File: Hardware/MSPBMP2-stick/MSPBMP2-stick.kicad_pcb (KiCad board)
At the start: 2 copper layers, 51.5 x 20 mm, 54 parts, among them J1 48037-0001, J2 JTAG, J3 SWD, U1 STM32L432KBU6, U2 LD1117AG-33-AB3-A-R, U3 AD8531ARTZ, U4 TXS0108EPWR, Y1 32768

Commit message: Schema update of PCB-Stick
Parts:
- removed the C2 at (85.0, 61.8)
- removed the R11 at (104.6, 68.8)
- removed the R7 at (85.0, 60.8)
- added C6: 220nF, Capacitor_SMD:C_0402_1005Metric_Pad0.74x0.62mm_HandSolder, F.Cu at (85.0, 62.8)
- added R4: 100, Resistor_SMD:R_0402_1005Metric_Pad0.72x0.64mm_HandSolder, F.Cu at (85.0, 61.8)
- C1: value 220nF -> 100nF
- C12: renamed from C10; value 1.2pF -> 4.7pF
- C13: renamed from C11; value 1.2pF -> 4.7pF
- RN1, RN2: footprint Resistor_SMD:R_Array_Convex_4x0402 -> LocalLib:R_Array_Convex_4x0402_hand_soldered
- U1: renamed from U2; value LD1117AG-33-AB3-A-R -> AMS1117-3.3
- U3: footprint Package_TO_SOT_SMD:TSOT-23-5_HandSoldering -> Package_TO_SOT_SMD:SOT-23-5_HandSoldering
- Y1: value 32768 -> 32768 7pF
- moved C16 4.27 mm to (96.2, 66.3), turned to 0 degrees
- moved C15 4.16 mm to (96.8, 67.5), turned to 0 degrees
- moved C19 1.54 mm to (96.1, 56.8)
- moved C17 1.23 mm to (95.5, 55.5)
- moved NT1 1.07 mm to (87.1, 62.8)
- moved F1 0.60 mm to (103.0, 56.5)
- moved C23 0.29 mm to (77.9, 54.1)
- moved U4 0.06 mm to (102.4, 64.7), turned to 180 degrees
- renumbered C13 to C10, C8 to C11, C3 to C2, C4 to C3, C6 to C4, C9 to C5, C12 to C7, C5 to C8, C7 to C9, R2 to R1, R10 to R11, R3 to R2, R1 to R3, R4 to R5, R5 to R7, R9 to R8, R8 to R9, U1 to U2
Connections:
- C15 pad 1: +3V3 -> GND
- C15 pad 2: GND -> +3V3
- C16 pad 1: +3V3 -> GND
- C16 pad 2: GND -> +3V3
- RN1 pad 1: Net-(RN1-Pad1) -> /LTDO
- RN1 pad 2: Net-(RN1-Pad2) -> /LTDI
- RN1 pad 3: Net-(RN1-Pad3) -> /LTMS
- RN1 pad 4: Net-(RN1-Pad4) -> /LTCK
- RN2 pad 1: Net-(RN2-Pad1) -> /LTEST
- RN2 pad 2: Net-(RN2-Pad2) -> /LRST
- RN2 pad 3: Net-(RN2-Pad3) -> /LTXD
- RN2 pad 4: Net-(RN2-Pad4) -> /LRXD
- U2 pad 15: /JENA -> Net-(U2-Pad15)
- U4 pad 1: /JTDO -> /LRXD
- U4 pad 10: /JENA -> /VCC_TOOL
- U4 pad 12: Net-(RN2-Pad4) -> /JTDO
- U4 pad 13: Net-(RN2-Pad3) -> /JTDI
- U4 pad 14: Net-(RN2-Pad2) -> /JTMS
- U4 pad 15: Net-(RN2-Pad1) -> /JTCK
- U4 pad 16: Net-(RN1-Pad4) -> /JTEST
- U4 pad 17: Net-(RN1-Pad3) -> /JRST
- U4 pad 18: Net-(RN1-Pad2) -> /JTXD
- U4 pad 19: /VCC_TOOL -> +3V3
- U4 pad 2: +3V3 -> /VCC_TOOL
- U4 pad 20: Net-(RN1-Pad1) -> /JRXD
- U4 pad 3: /JTDI -> /LTXD
- U4 pad 4: /JTMS -> /LRST
- U4 pad 5: /JTCK -> /LTEST
- U4 pad 6: /JTEST -> /LTCK
- U4 pad 7: /JRST -> /LTMS
- U4 pad 8: /JRXD -> /LTDI
- U4 pad 9: /JTXD -> /LTDO
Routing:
- net /JENA: track 33.3 -> 0.00 mm, vias 2 -> 0
- net GND: track 44.0 -> 37.3 mm, vias 16 -> 15
- net Net-(RN1-Pad2): track 4.36 -> 0.00 mm
- net Net-(RN1-Pad3): track 4.30 -> 0.00 mm
- net /VCC_TOOL: track 20.4 -> 24.6 mm
- net Net-(RN1-Pad4): track 4.17 -> 0.00 mm
- net /LTMS: track 0.00 -> 4.17 mm
- net /LTCK: track 0.00 -> 4.11 mm
- net /LTDI: track 0.00 -> 4.10 mm
- net /LTDO: track 0.00 -> 3.90 mm
- net +3V3: track 111.0 -> 114.3 mm
- net Net-(RN1-Pad1): track 3.20 -> 0.00 mm
- net /LRXD: track 0.00 -> 2.71 mm
- net Net-(RN2-Pad4): track 2.49 -> 0.00 mm
- net Net-(RN2-Pad1): track 2.47 -> 0.00 mm
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
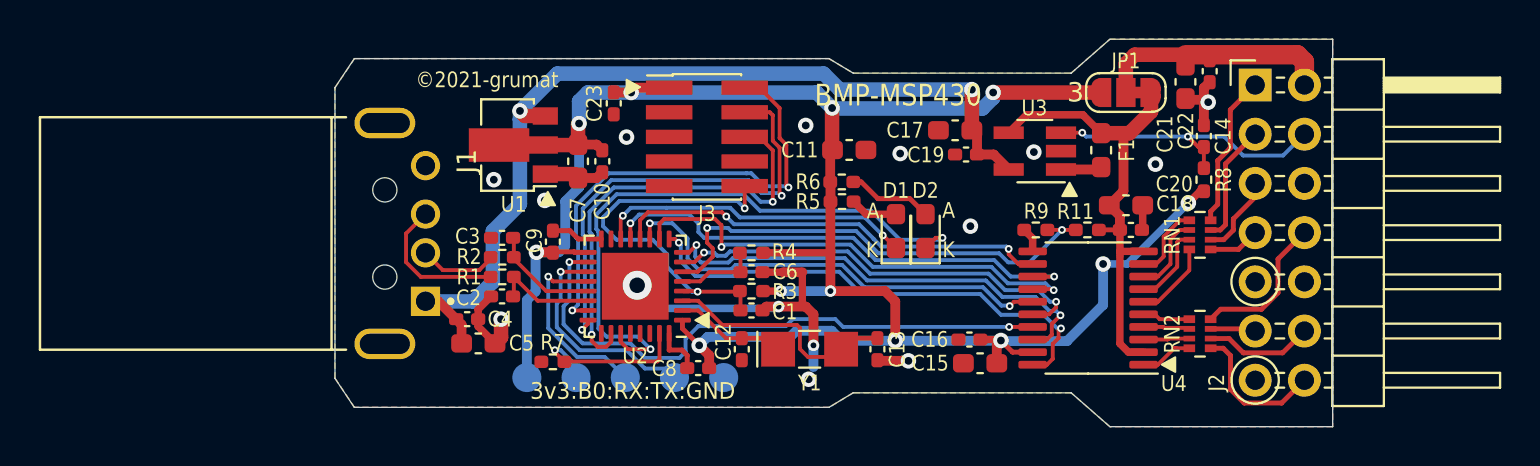
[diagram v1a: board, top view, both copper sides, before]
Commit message: Hardware V2 improvements (component values and sizes, layout and review of V-Target circuitry).
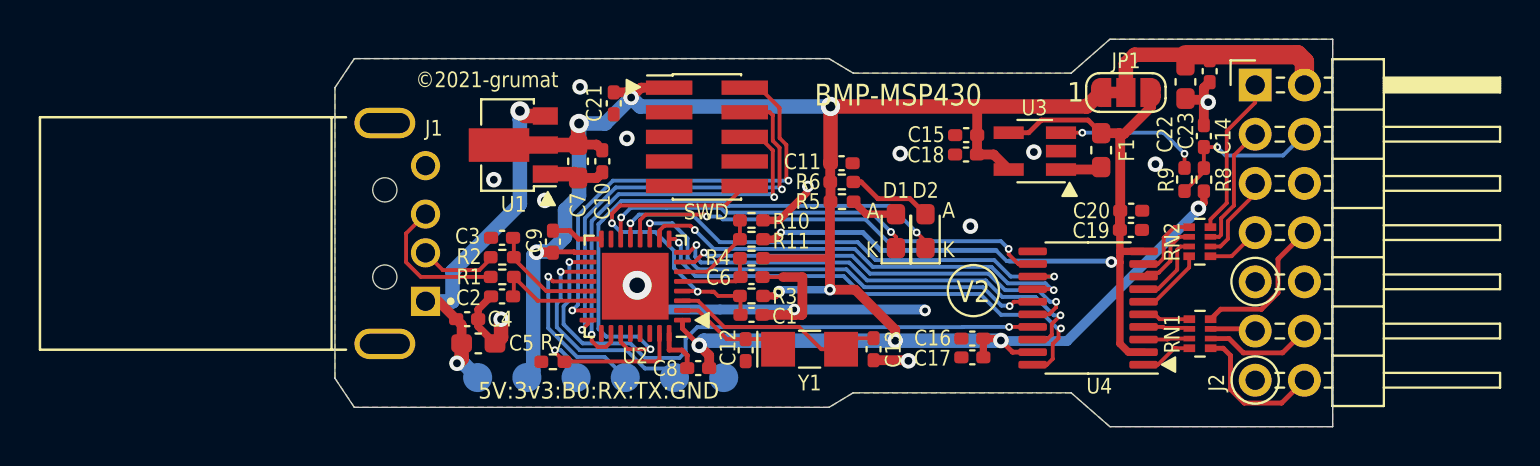
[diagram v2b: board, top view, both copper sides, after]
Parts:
- added R9: 4k7, Resistor_SMD:R_0402_1005Metric_Pad0.72x0.64mm_HandSolder, F.Cu at (107.3, 58.0)
- added TP1: 5V, TestPoint:TestPoint_Pad_D1.5mm, B.Cu at (70.9, 68.3)
- C11, C20: value 22uF -> 10uF; footprint Capacitor_SMD:C_0603_1608Metric_Pad1.08x0.95mm_HandSolder -> Capacitor_SMD:C_0402_1005Metric_Pad0.74x0.62mm_HandSolder
- C15: renamed from C17; value 22uF -> 10uF; footprint Capacitor_SMD:C_0603_1608Metric_Pad1.08x0.95mm_HandSolder -> Capacitor_SMD:C_0402_1005Metric_Pad0.74x0.62mm_HandSolder
- C16: renamed from C15; value 22uF -> 10uF; footprint Capacitor_SMD:C_0603_1608Metric_Pad1.08x0.95mm_HandSolder -> Capacitor_SMD:C_0402_1005Metric_Pad0.74x0.62mm_HandSolder
- moved R11 17.3 mm to (85.0, 61.1)
- moved R10 14.7 mm to (85.0, 60.1), turned to 0 degrees
- moved C16 1.34 mm to (96.4, 66.2)
- moved C17 0.93 mm to (96.4, 67.2)
- moved C11 0.79 mm to (89.7, 57.2)
- moved C15 0.62 mm to (96.1, 55.8)
- moved C20 0.39 mm to (104.6, 59.6)
- moved RN2 0.35 mm to (108.1, 61.2)
- moved R4 0.27 mm to (85.0, 62.1)
- moved C6 0.25 mm to (85.0, 63.1)
- moved NT1 0.25 mm to (87.1, 63.1)
- moved R3 0.25 mm to (85.0, 64.0)
- moved C1 0.23 mm to (85.0, 65.0)
- moved C12 0.21 mm to (84.7, 66.8)
- moved C13 0.20 mm to (91.3, 66.8)
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- renumbered C16 to C17, C19 to C18, C18 to C19, C23 to C21, C21 to C22, C22 to C23, R9 to R10, RN2 to RN1, RN1 to RN2, TP1 to TP2, TP2 to TP3, TP3 to TP4, TP4 to TP5, TP5 to TP6
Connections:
- C15 pad 1: +5V -> +3V3
- C18 pad 2: +5V -> +3V3
- JP1 pad 1: /VCC_TOOL -> +3V3
- JP1 pad 3: +3V3 -> /VCC_TOOL
- U3 pad 3: /TVCC -> Net-(R9-Pad1)
- U3 pad 5: +5V -> +3V3
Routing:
- net +5V: track 47.9 -> 19.9 mm
- net /VREF2: track 24.7 -> 4.63 mm, vias 2 -> 0
- net /VCC_TOOL: track 24.6 -> 41.9 mm, vias 0 -> 2
- net Net-(R9-Pad1): track 0.00 -> 7.56 mm, vias 0 -> 2
- net /TVCC: track 15.6 -> 8.51 mm, vias 2 -> 1
- net GND: track 37.3 -> 40.5 mm
- net /LED_RED: track 31.6 -> 29.3 mm
- net /NRST: track 20.1 -> 18.4 mm
- net /SWDIO: track 24.9 -> 23.6 mm
- net /JTMS: track 24.6 -> 23.4 mm
- net /SWCLK: track 24.1 -> 22.9 mm
- net /OSC_OUT: track 12.3 -> 11.1 mm
- net /TRACESWO: track 23.1 -> 22.1 mm
- net +3V3: track 114.3 -> 115.1 mm, vias 12 -> 10
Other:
- board text added: "5V:3v3:B0:RX:TX:GND"
- board text added: "V2"
- board text removed: "3v3:B0:RX:TX:GND"

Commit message: New Hardware layout to it SWD connector in case.
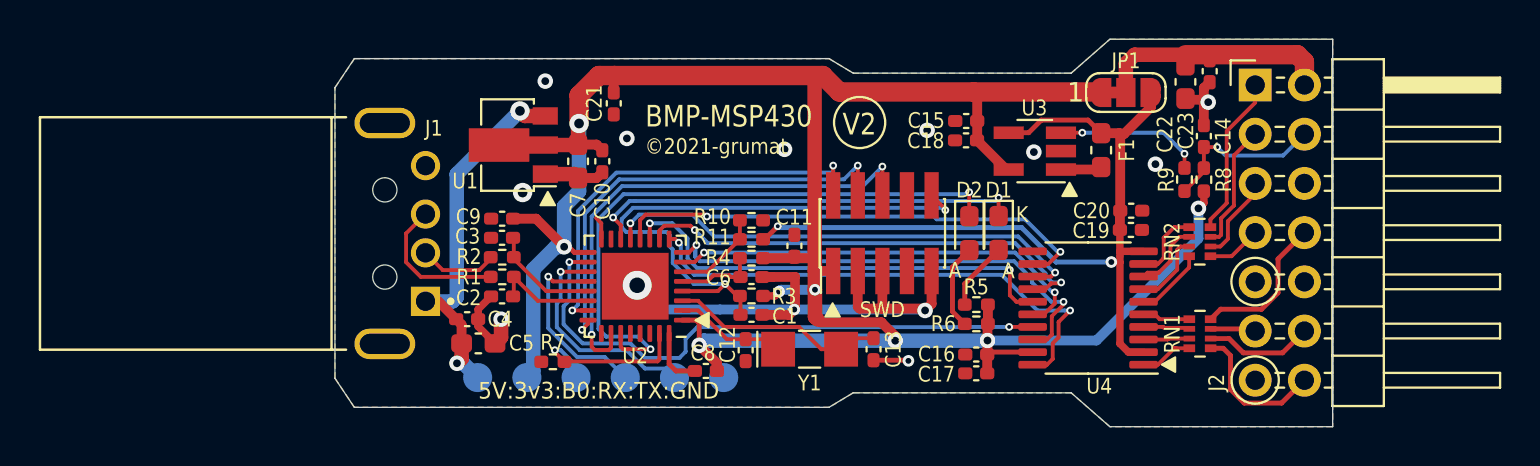
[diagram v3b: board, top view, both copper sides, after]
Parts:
- moved J3 10.3 mm to (91.8, 60.8), turned to 90 degrees
- moved R6 10.1 mm to (96.6, 65.5), turned to 0 degrees
- moved R5 8.74 mm to (96.6, 64.5), turned to 0 degrees
- moved D1 5.30 mm to (97.8, 60.8), turned to 270 degrees
- moved C11 4.91 mm to (87.2, 61.5), turned to 90 degrees
- moved C9 2.88 mm to (72.1, 60.1), turned to 180 degrees
- moved D2 2.27 mm to (96.2, 60.8), turned to 270 degrees
- moved C16 0.85 mm to (96.6, 67.1)
- moved C17 0.85 mm to (96.6, 68.0)
- moved C15 0.73 mm to (96.1, 55.0)
- moved C18 0.73 mm to (96.1, 56.0)
- moved NT1 0.51 mm to (87.2, 63.6), turned to 90 degrees
- moved C8 0.42 mm to (82.6, 67.9)
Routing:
- net /NRST: track 18.4 -> 30.1 mm
- net +3V3: track 115.1 -> 122.5 mm, vias 10 -> 8
- net /LED_GREEN: track 16.7 -> 22.5 mm
- net GND: track 40.5 -> 44.6 mm, vias 15 -> 13
- net /TRACESWO: track 22.1 -> 26.1 mm
- net /LED_RED: track 29.3 -> 32.0 mm
- net /JTDO: track 22.6 -> 25.3 mm
- net /SWDIO: track 23.6 -> 22.0 mm
- net Net-(D1-Pad2): track 2.45 -> 3.91 mm
- net /JTXD: track 23.9 -> 25.3 mm
- net /JRXD: track 25.6 -> 26.8 mm
- net /JTMS: track 23.4 -> 24.2 mm
- net GNDA: track 1.06 -> 1.68 mm
- net /JTCK: track 23.0 -> 23.6 mm

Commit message: Upgrade MSPBMP2-stick.pro to KiCad 6
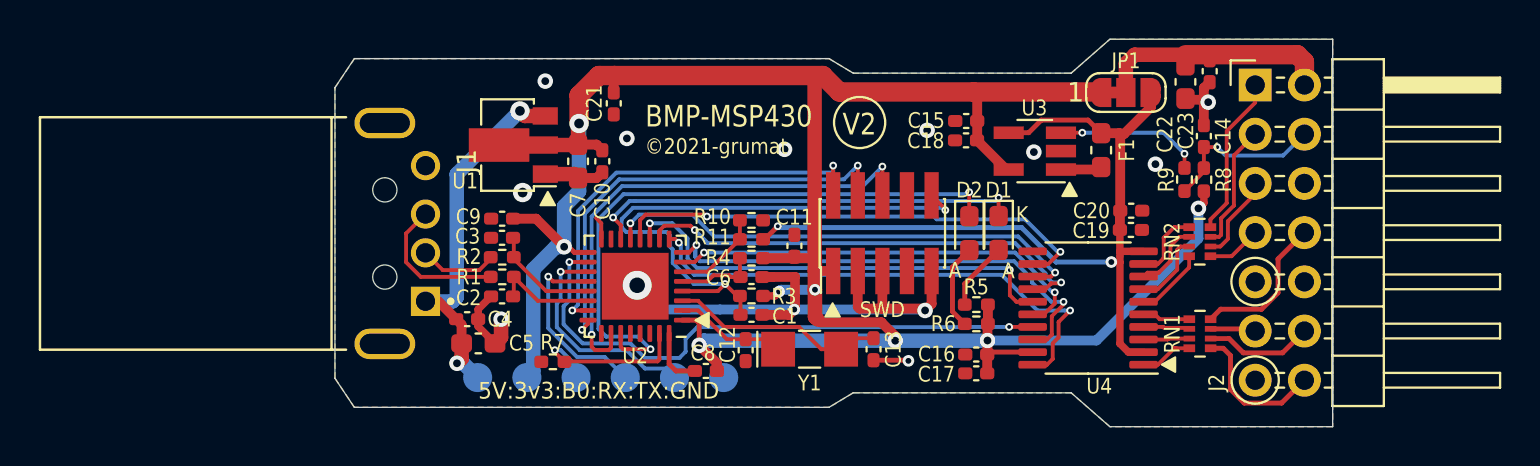
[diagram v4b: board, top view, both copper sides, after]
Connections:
- J2 pad 10: Net-(J2-Pad10) -> unconnected-(J2-Pad10)
- J2 pad 6: Net-(J2-Pad6) -> unconnected-(J2-Pad6)
- J3 pad 7: Net-(J3-Pad7) -> unconnected-(J3-Pad7)
- J3 pad 8: Net-(J3-Pad8) -> unconnected-(J3-Pad8)
- U2 pad 15: Net-(U2-Pad15) -> unconnected-(U2-Pad15)
- U2 pad 25: Net-(U2-Pad25) -> unconnected-(U2-Pad25)
- U2 pad 28: Net-(U2-Pad28) -> unconnected-(U2-Pad28)
- U2 pad 29: Net-(U2-Pad29) -> unconnected-(U2-Pad29)
- U2 pad 30: Net-(U2-Pad30) -> unconnected-(U2-Pad30)
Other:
- net class Analog removed
- net class Default removed
- net class Power removed
